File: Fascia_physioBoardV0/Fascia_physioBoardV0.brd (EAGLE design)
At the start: 37.3 x 39.1 mm, 88 parts, among them CN2 CA0612KRX7R9BB102, CN3 CA0612KRX7R9BB102, CN4 CA0612KRX7R9BB102, CN5 CA0612KRX7R9BB102, CN6 CA0612KRX7R9BB102, J1 MOLEX_52437-2471MOLEX_52437-2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, J2 MOLEX_52437-2471MOLEX_52437-2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, J3 MOLEX_51296-1294MOLEX_51296-1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, U1 ADS1299-X, U10 TPD4E1B06DCKR, U11 TPD4E1B06DCKR, U12 OPA320AIDBVRDBV5-L, U13 ADUM5028, U2 OPA2320AIDGKT_NOVA8-SOIC-L, U3 OPA2320AIDGKT_NOVAL8-SOIC-L, U4 HCNR200-300E, U5 OPA320AIDBVRDBV5-L, U6 TPD4E1B06DCKR, U7 TPD4E1B06DCKR, U8 TPD4E1B06DCKR, U9 TPD4E1B06DCKR

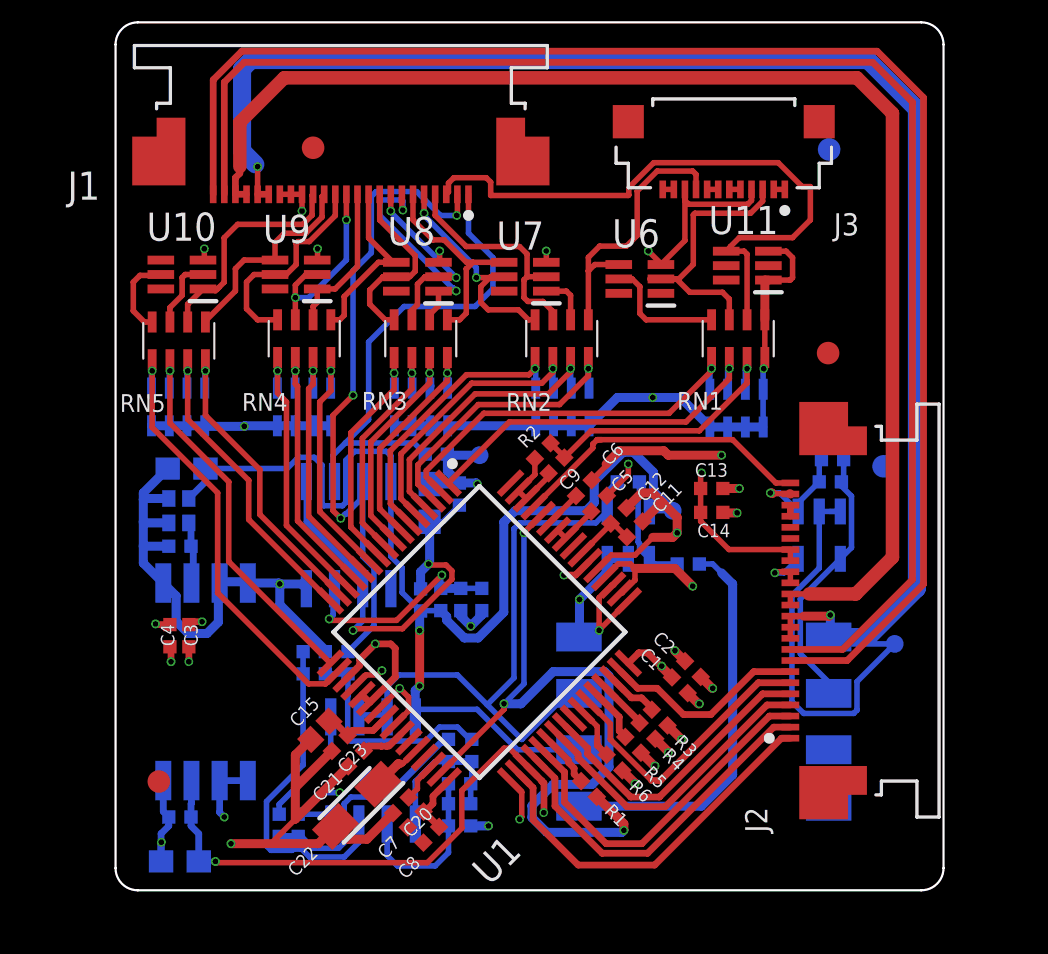
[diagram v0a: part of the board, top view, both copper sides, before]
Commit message: fixed some traces and completed board traces
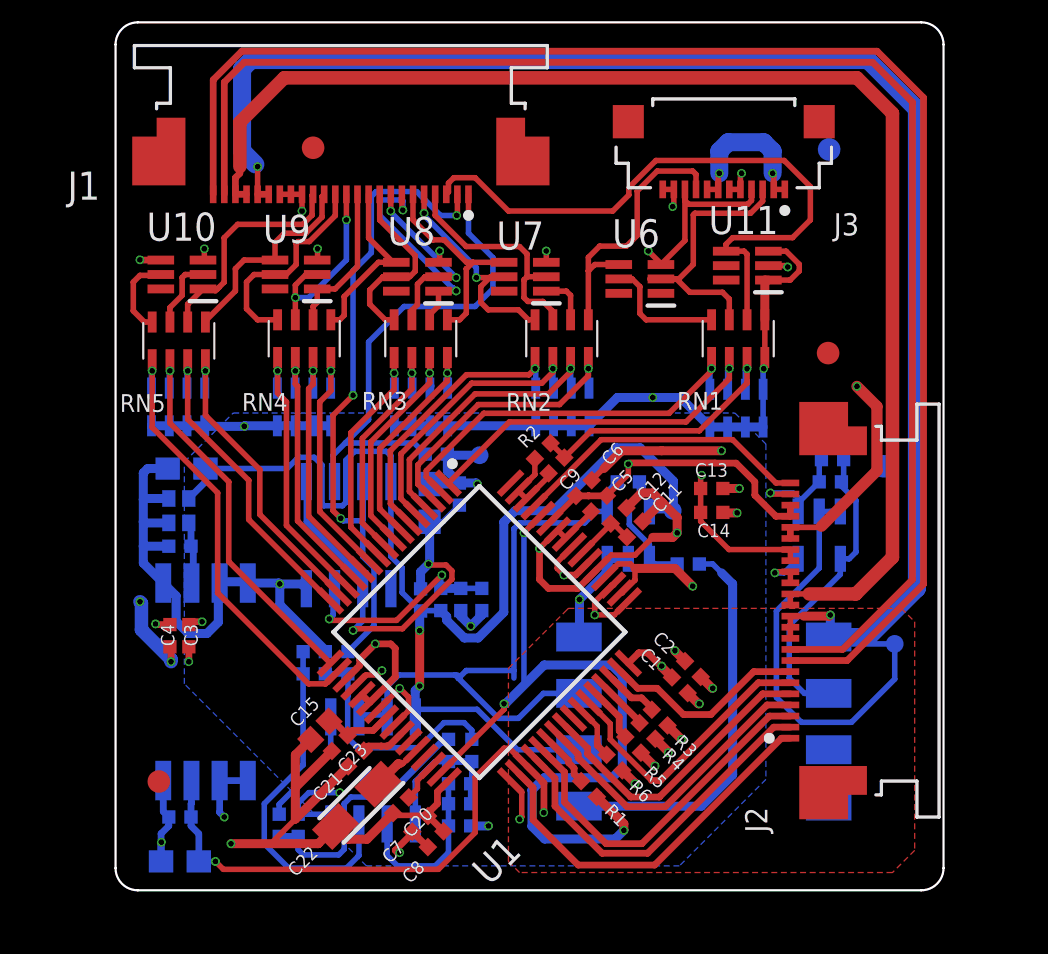
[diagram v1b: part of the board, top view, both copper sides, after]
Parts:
- moved C8 0.28 mm to (17.1, 3.50)
- moved C7 0.28 mm to (16.4, 4.19)
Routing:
- net AVDD: track 14.2 -> 60.1 mm, vias 5 -> 9
- net AVSS: track 51.0 -> 93.9 mm, vias 9 -> 15
- net AGND: track 90.1 -> 92.5 mm
- net N$9: track 12.2 -> 13.7 mm
- net GND_ISO: track 40.6 -> 41.4 mm
- net N$3: track 14.9 -> 15.8 mm
- net N$4: track 11.7 -> 12.5 mm
- net DVDD: track 36.4 -> 37.2 mm
- net EDA-: track 31.2 -> 31.8 mm
- net GND: track 107.6 -> 108.2 mm
- net N$1: track 10.0 -> 10.7 mm
- net N$12: track 19.4 -> 19.9 mm
- added copper zone on layer 16, net DVDD_ISO
- added copper zone on layer 1, net GND

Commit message: minor change
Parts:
- moved RAW_EDA_SIG 4.08 mm to (11.7, 2.90)
- moved GND_ISO 0.70 mm to (19.8, 20.8)
- moved CN2 0.05 mm to (30.7, 23.0)
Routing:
- net N$3: track 15.8 -> 16.6 mm
- net GND_ISO: track 41.4 -> 42.1 mm
- net N$4: track 12.5 -> 13.0 mm

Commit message: MINOR CHANGES
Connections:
- net ADS_RESET2 renamed ADS_RESET
- net PA20_CS2 renamed PA20_CS
- net BIAS_INV: no longer J2.24
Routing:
- net BIAS_INV: track 13.6 -> 18.6 mm
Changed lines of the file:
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@@
 <drawing>
 <settings>
-<setting alwaysvectorfont="yes"/>
+<setting alwaysvectorfont="no"/>
 <setting verticaltext="up"/>
 </settings>
@@
 <signal name="BIAS_INV">
 <contactref element="U1" pad="61"/>
-<contactref element="J2" pad="24"/>
 <wire x1="21.557309375" y1="18.481715625" x2="24.57559375" y2="21.5" width="0.25" layer="1"/>
-<wire x1="33.1" y1="19.55" x2="32.45" y2="19.55" width="0.25" layer="1"/>
-<wire x1="30.5" y1="21.5" x2="24.57559375" y2="21.5" width="0.25" layer="1"/>
-<wire x1="32.45" y1="19.55" x2="30.5" y2="21.5" width="0.25" layer="1"/>
+<wire x1="24.57559375" y1="21.5" x2="29.6" y2="21.5" width="0.25" layer="1"/>
+<wire x1="29.6" y1="21.5" x2="33.1" y2="25" width="0.25" layer="1"/>
+<wire x1="33.1" y1="25" x2="33.1" y2="26.7" width="0.25" layer="1"/>
+<wire x1="33.1" y1="26.7" x2="34.8" y2="28.4" width="0.25" layer="1"/>
+<wire x1="34.8" y1="28.4" x2="35.1" y2="28.4" width="0.25" layer="1"/>
 </signal>
 <signal name="IN8N">
@@
 <wire x1="38.6" y1="36.7" x2="36.8" y2="38.5" width="0.3048" layer="1"/>
 </signal>
-<signal name="PA20_CS2">
+<signal name="PA20_CS">
 <contactref element="U1" pad="39"/>
 <wire x1="23.5364" y1="7.16365" x2="25.73185" y2="4.9682" width="0.3048" layer="1"/>
@@
 <wire x1="8.1" y1="32.554" x2="8.6" y2="32.554" width="0.3048" layer="1"/>
 </signal>
-<signal name="ADS_RESET2">
+<signal name="ADS_RESET">
 <contactref element="U1" pad="36"/>
 <contactref element="J2" pad="2"/>

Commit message: files ready for manufacture
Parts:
- moved FD1 0.91 mm to (33.9, 34.5)
- moved J3 0.91 mm to (29.2, 34.2)
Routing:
- net S0_I2C_SCL: track 65.5 -> 63.7 mm
- net S0_I2C_SDA: track 67.9 -> 66.2 mm
- net VCC: track 60.6 -> 59.0 mm
- net GND: track 108.2 -> 106.8 mm
- net BIAS: track 29.2 -> 27.8 mm
- net 8N: track 12.8 -> 11.7 mm
- net 7N: track 12.7 -> 11.7 mm
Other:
- outline, holes or cut-outs redrawn
- board text added: "FACIA_MAINBOARD_V0_11/21/19"
